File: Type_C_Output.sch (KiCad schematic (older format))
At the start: 38 parts, among them J1 USB_C_Receptacle_USB2.0, Q18 VBA2625, Q19 VBA2625, Q20 VBA2625, Q21 2n7002K, U12 STUSB4700

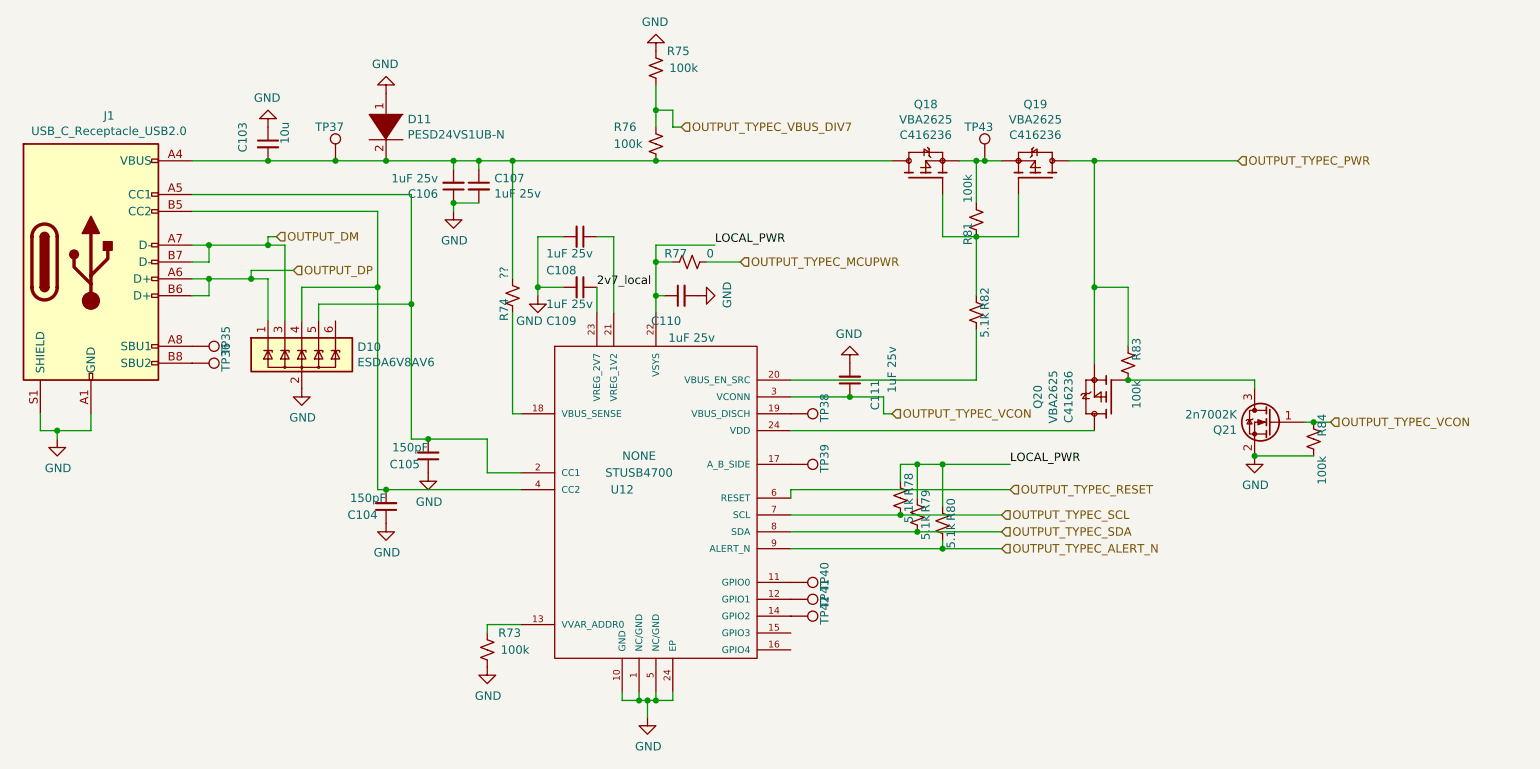
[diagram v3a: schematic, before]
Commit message: Almost connected MCU + ESP32 added leds addedd uart usb cleaned up type-c I/O -- STILL NEED TO level shift I2C
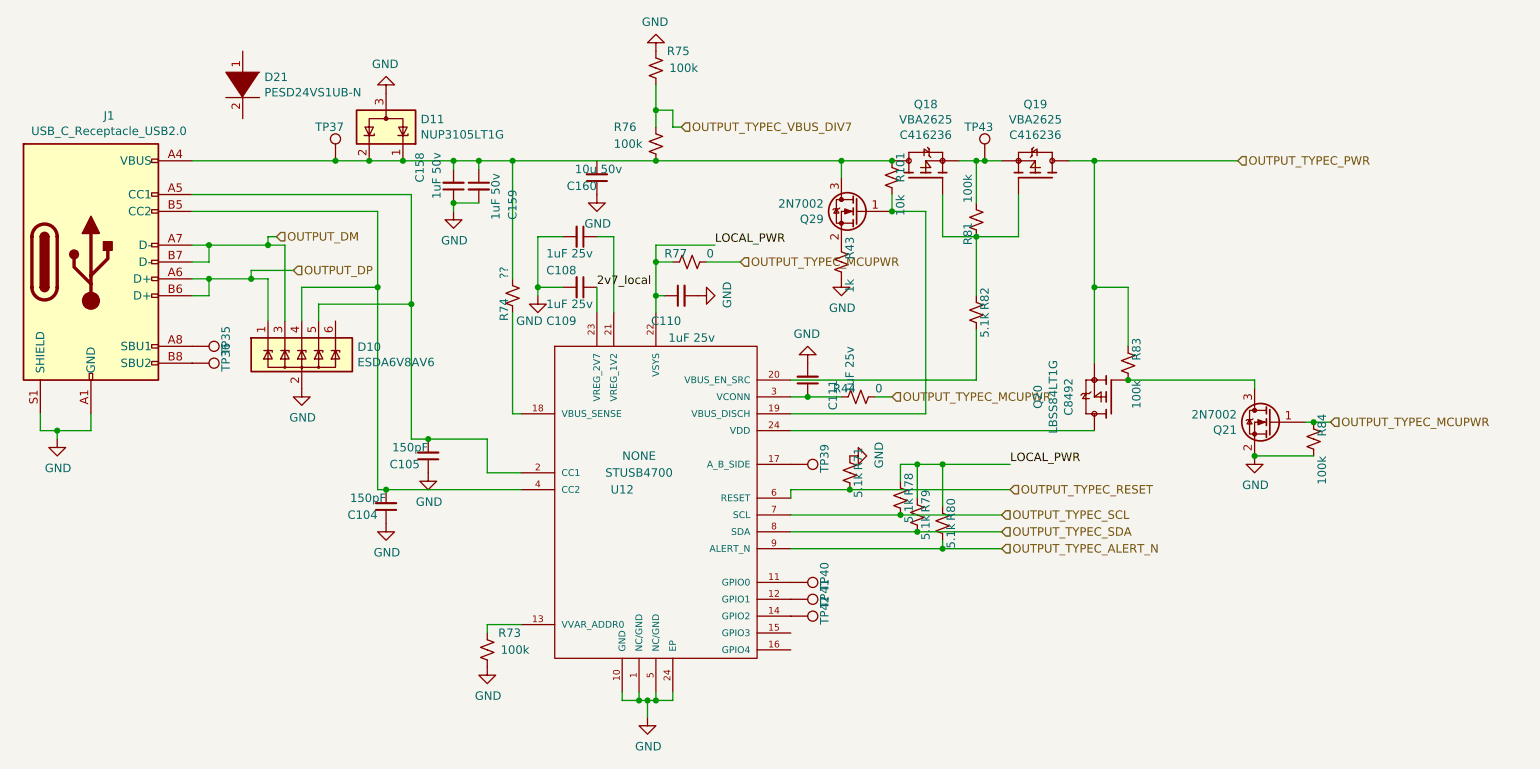
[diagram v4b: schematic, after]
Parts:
- removed C103: 10u, lc_lib:0805_C, symbol Device:C_Small
- removed C106, C107: 1uF 25v, lc_lib:0402_C, symbol Device:C_Small
- removed D11: PESD24VS1UB-N, lc_lib:SOD-523, symbol pspice:DIODE
- removed TP38: TestPoint, TestPoint:TestPoint_Pad_D2.0mm, symbol Connector:TestPoint
- added C158, C159: 1uF 50v, lc_lib:0603_C, symbol Device:C_Small
- added C160: 10u 50v, lc_lib:0805_C, symbol Device:C_Small
- added D11: NUP3105LT1G, Package_TO_SOT_SMD:SOT-23, symbol Power_Protection:SP0502BAJT
- added D21: PESD24VS1UB-N, lc_lib:SOD-523, symbol pspice:DIODE
- added Q29: 2N7002, Package_TO_SOT_SMD:SOT-23, symbol Device:Q_NMOS_GSD
- added R101: 10k, lc_lib:0402_R, symbol Device:R_Small_US
- added R43: 1k, lc_lib:0402_R, symbol Device:R_Small_US
- added R44: 0, lc_lib:0402_R, symbol Device:R_Small_US
- added R71: 5.1k, lc_lib:0402_R, symbol Device:R_Small_US
- Q20: value VBA2625 -> LBSS84LT1G; footprint SmartBattery:SOIC127P600X175-8N -> lc_lib:SOT-23(SOT-23-3); MANUFACTURER Alpha & Omega Semiconductor -> (none); MAXIMUM_PACKAGE_HEIGHT 1.75 mm -> (none); PARTREV I -> (none); STANDARD IPC 7351B -> (none); lcsc C416236 -> C8492
- Q21: value 2n7002K -> 2N7002; LCSC (none) -> C8545
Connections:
- net GND: now also C158.1, C159.2, C160.1, D11.3 (A), R43.1, R71.2
- net OUTPUT_TYPEC_MCUPWR: now also Q21.1 (G), R84.2, R44.1
- net OUTPUT_TYPEC_RESET: now also R71.1
- net at J1.A4 (VBUS), J1.A9 (VBUS), J1.B4 (VBUS)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: now also C158.2, C159.1, D11.1 (K), D11.2 (K), Q29.3 (D), R101.2
- net at U12.19 (VBUS_DISCH): now also Q29.1 (G), R101.1
- net OUTPUT_TYPEC_VCON: no longer names the net of C111.1, U12.3 (VCONN)
- net OUTPUT_TYPEC_VCON: now also R44.2; no longer Q21.1 (G), R84.2
- new net: Q29.2 (S), R43.2
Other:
- moved on the sheet: C111

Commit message: lots of GPIO connectivity changes. fixed no PD on input fixed CH340G leakage. can otherwise power from GPIO. added fet for powering VCONN from 3v/5v NEED TO ADD OVERCURRENT
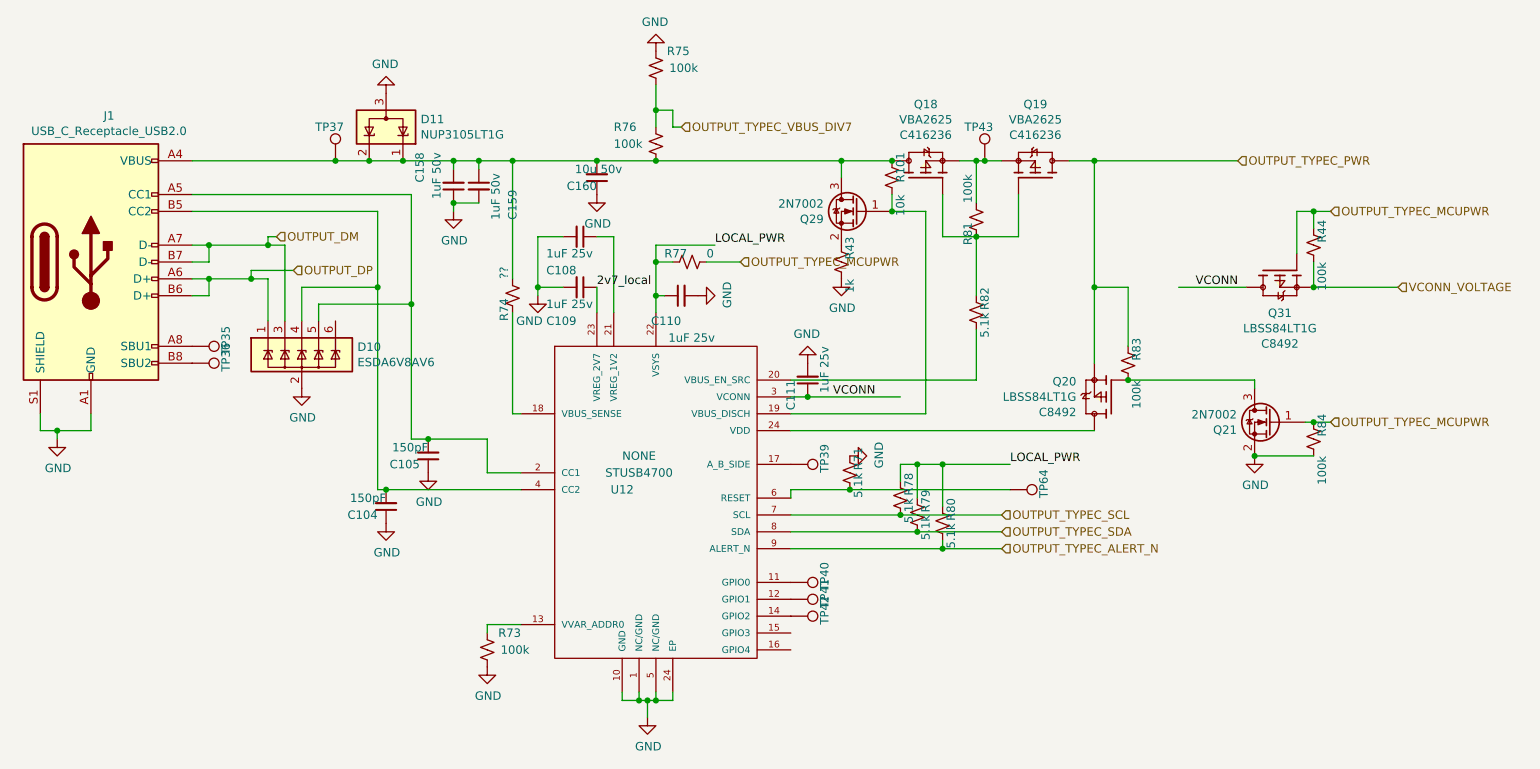
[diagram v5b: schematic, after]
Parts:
- removed D21: PESD24VS1UB-N, lc_lib:SOD-523, symbol pspice:DIODE
- removed Q20: LBSS84LT1G, lc_lib:SOT-23(SOT-23-3), symbol SmartBattery:VBA2625
- added Q20, Q31: LBSS84LT1G, lc_lib:SOT-23(SOT-23-3), symbol SmartBattery:LBSS84LT1G
- added TP64: TestPoint, TestPoint:TestPoint_Pad_D2.0mm, symbol Connector:TestPoint
- R44: value 0 -> 100k; LCSC (none) -> C25741
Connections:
- net OUTPUT_TYPEC_MCUPWR: now also R44.2, Q31.1; no longer R44.1
- net OUTPUT_TYPEC_PWR: now also Q20.2
- net at C158.2, C159.1, D11.1 (K)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: now also C160.2
- net VCONN: now reaches C111.1, U12.3 (VCONN)
- net VCONN: now also Q31.3; no longer R44.2
- net at Q21.3 (D), R83.1: now also Q20.1
- net OUTPUT_TYPEC_RESET: no longer names the net of R71.1, U12.6 (RESET)
- net OUTPUT_TYPEC_RESET: now also TP64.1
- new net: Q20.3, U12.24 (VDD)
- new net VCONN_VOLTAGE: Q31.2, R44.1
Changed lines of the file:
@@
 Connection ~ 4050 1550
 Wire Wire Line
-	4050 1550 4900 1550
+	4050 1550 4550 1550
 Wire Wire Line
 	3850 1600 3850 1550
@@
 Wire Wire Line
 	5700 3150 7500 3150
-$Comp
-L SmartBattery:VBA2625 Q?
-U 1 1 60201E98
-P 7600 2950
-AR Path="/5FF971C1/60201E98" Ref="Q?"  Part="1"
-AR Path="/600C8F88/60201E98" Ref="Q20"  Part="1"
-F 0 "Q20" V 8035 2950 50  0000 C CNN
-F 1 "LBSS84LT1G" V 7944 2950 50  0000 C CNN
-F 2 "lc_lib:SOT-23(SOT-23-3)" H 7600 2950 50  0001 L BNN
-F 3 "" H 7600 2950 50  0001 L BNN
-F 4 "" H 7600 2950 50  0001 L BNN "MANUFACTURER"
-F 5 "" H 7600 2950 50  0001 L BNN "PARTREV"
-F 6 "" H 7600 2950 50  0001 L BNN "STANDARD"
-F 7 "" H 7600 2950 50  0001 L BNN "MAXIMUM_PACKAGE_HEIGHT"
-F 8 "C8492" V 7853 2950 50  0000 C CNN "lcsc"
-	1    7600 2950
-	-1   0    0    -1
-$EndComp
 Text Label 5250 2050 0    50   ~ 0
 LOCAL_PWR
@@
 Wire Wire Line
 	5700 3650 6350 3650
-Text HLabel 7000 3500 2    50   Input ~ 0
-OUTPUT_TYPEC_RESET
 Wire Wire Line
 	7000 3500 6050 3500
@@
 AR Path="/5FF971C1/60269C14" Ref="C?"  Part="1"
 AR Path="/600C8F88/60269C14" Ref="C111"  Part="1"
-F 0 "C111" V 5650 2850 50  0000 L CNN
-F 1 "1uF 25v" V 5550 2650 50  0000 L CNN
+F 0 "C111" V 5900 2850 50  0000 L CNN
+F 1 "1uF 25v" V 5700 2650 50  0000 L CNN
 F 2 "lc_lib:0402_C" H 5800 2850 50  0001 C CNN
 F 3 "~" H 5800 2850 50  0001 C CNN
@@
 $EndComp
 Connection ~ 5800 2950
-Wire Wire Line
-	5800 2950 6000 2950
 $Comp
 L power:GND #PWR?
@@
 	-1   0    0    1
 $EndComp
-Text HLabel 6300 2950 2    50   Input ~ 0
+Text HLabel 8900 1850 2    50   Input ~ 0
 OUTPUT_TYPEC_MCUPWR
 Wire Wire Line
@@
 Wire Wire Line
 	8450 2850 8450 2900
-Connection ~ 7700 2850
 $Comp
 L power:GND #PWR?
@@
 Connection ~ 3400 1550
 $Comp
-L Device:R_Small_US R?
-U 1 1 60344C8C
-P 6100 2950
-AR Path="/5FD99B08/60344C8C" Ref="R?"  Part="1"
-AR Path="/5FF1D194/60344C8C" Ref="R?"  Part="1"
-AR Path="/600C8F88/60344C8C" Ref="R44"  Part="1"
-F 0 "R44" V 6050 2800 50  0000 L CNN
-F 1 "0" V 6050 3050 50  0000 L CNN
-F 2 "lc_lib:0402_R" H 6100 2950 50  0001 C CNN
-F 3 "~" H 6100 2950 50  0001 C CNN
-	1    6100 2950
-	0    1    1    0
-$EndComp
-$Comp
 L Device:Q_NMOS_GSD Q?
 U 1 1 6034DD17
@@
 $EndComp
 Wire Wire Line
-	6200 2950 6300 2950
-Wire Wire Line
 	5700 3050 6500 3050
 Wire Wire Line
@@
 	1    3900 3250
 	1    0    0    -1
-$EndComp
-$Comp
-L pspice:DIODE D?
-U 1 1 60206BB7
-P 2450 1100
-AR Path="/5FF971C1/60206BB7" Ref="D?"  Part="1"
-AR Path="/600C8F88/60206BB7" Ref="D21"  Part="1"
-F 0 "D21" V 2404 1228 50  0000 L CNN
-F 1 "PESD24VS1UB-N" V 2495 1228 50  0000 L CNN
-F 2 "lc_lib:SOD-523" H 2450 1100 50  0001 C CNN
-F 3 "~" H 2450 1100 50  0001 C CNN
-F 4 "C316036" V 2450 1100 50  0001 C CNN "lcsc"
-	1    2450 1100
-	0    1    1    0
 $EndComp
 $Comp
@@
 	0    -1   -1   0
 $EndComp
+$Comp
+L Connector:TestPoint TP?
+U 1 1 6026B3C6
+P 7000 3500
+AR Path="/5FD15753/6026B3C6" Ref="TP?"  Part="1"
+AR Path="/5FD99B08/6026B3C6" Ref="TP?"  Part="1"
+AR Path="/5FF971C1/6026B3C6" Ref="TP?"  Part="1"
+AR Path="/600C8F88/6026B3C6" Ref="TP64"  Part="1"
+F 0 "TP64" H 7050 3700 50  0000 R CNN
+F 1 "TestPoint" H 6450 3550 50  0001 R CNN
+F 2 "TestPoint:TestPoint_Pad_D2.0mm" H 7200 3500 50  0001 C CNN
+F 3 "~" H 7200 3500 50  0001 C CNN
+	1    7000 3500
+	0    1    1    0
+$EndComp
+Connection ~ 4550 1550
+Wire Wire Line
+	4550 1550 4900 1550
+Wire Wire Line
+	5800 2950 6350 2950
+Text HLabel 9300 2300 2    50   Input ~ 0
+VCONN_VOLTAGE
+Text Label 5950 2950 0    50   ~ 0
+VCONN
+Wire Wire Line
+	8400 2300 8000 2300
+Text Label 8100 2300 0    50   ~ 0
+VCONN
+$Comp
+L SmartBattery:LBSS84LT1G Q20
+U 1 1 6036965C
+P 7600 2950
+F 0 "Q20" H 7807 3041 50  0000 L CNN
+F 1 "LBSS84LT1G" H 7807 2950 50  0000 L CNN
+F 2 "lc_lib:SOT-23(SOT-23-3)" H 7600 2950 50  0001 L BNN
+F 3 "" H 7600 2950 50  0001 L BNN
+F 4 "I" H 7600 2950 50  0001 L BNN "PARTREV"
+F 5 "IPC 7351B" H 7600 2950 50  0001 L BNN "STANDARD"
+F 6 "1.11 mm" H 7600 2950 50  0001 L BNN "MAXIMUM_PACKAGE_HEIGHT"
+F 7 "C8492" H 7807 2859 50  0000 L CNN "lcsc"
+	1    7600 2950
+	-1   0    0    -1
+$EndComp
+$Comp
+L SmartBattery:LBSS84LT1G Q31
+U 1 1 6036CF55
+P 8600 2200
+F 0 "Q31" V 8853 2200 50  0000 C CNN
+F 1 "LBSS84LT1G" V 8944 2200 50  0000 C CNN
+F 2 "lc_lib:SOT-23(SOT-23-3)" H 8600 2200 50  0001 L BNN
+F 3 "" H 8600 2200 50  0001 L BNN
+F 4 "I" H 8600 2200 50  0001 L BNN "PARTREV"
+F 5 "IPC 7351B" H 8600 2200 50  0001 L BNN "STANDARD"
+F 6 "1.11 mm" H 8600 2200 50  0001 L BNN "MAXIMUM_PACKAGE_HEIGHT"
+F 7 "C8492" V 9035 2200 50  0000 C CNN "lcsc"
+	1    8600 2200
+	0    1    1    0
+$EndComp
+Connection ~ 7700 2850
+Wire Wire Line
+	8700 2100 8700 1850
+Wire Wire Line
+	8700 1850 8800 1850
+Wire Wire Line
+	9300 2300 8800 2300
+$Comp
+L Device:R_Small_US R?
+U 1 1 60392469
+P 8800 2050
+AR Path="/5FD99B08/60392469" Ref="R?"  Part="1"
+AR Path="/5FF1D194/60392469" Ref="R?"  Part="1"
+AR Path="/5FF971C1/60392469" Ref="R?"  Part="1"
+AR Path="/600C8F88/60392469" Ref="R44"  Part="1"
+F 0 "R44" V 8750 1900 50  0000 L CNN
+F 1 "100k" V 8750 2150 50  0000 L CNN
+F 2 "lc_lib:0402_R" H 8800 2050 50  0001 C CNN
+F 3 "~" H 8800 2050 50  0001 C CNN
+F 4 "C25741" V 8800 2050 50  0001 C CNN "LCSC"
+	1    8800 2050
+	-1   0    0    1
+$EndComp
+Wire Wire Line
+	8800 1950 8800 1850
+Connection ~ 8800 1850
+Wire Wire Line
+	8800 1850 8900 1850
+Wire Wire Line
+	8800 2300 8800 2150
+Connection ~ 8800 2300
 $EndSCHEMATC

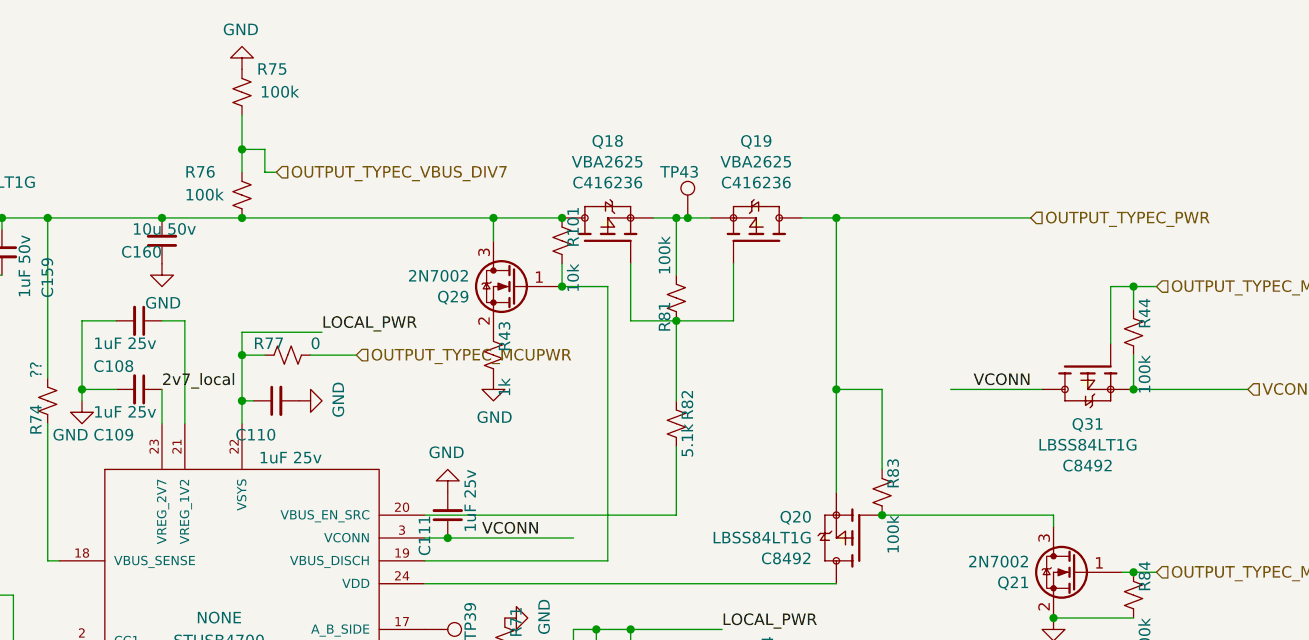
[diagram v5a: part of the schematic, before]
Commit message: Modified connections, added current limit
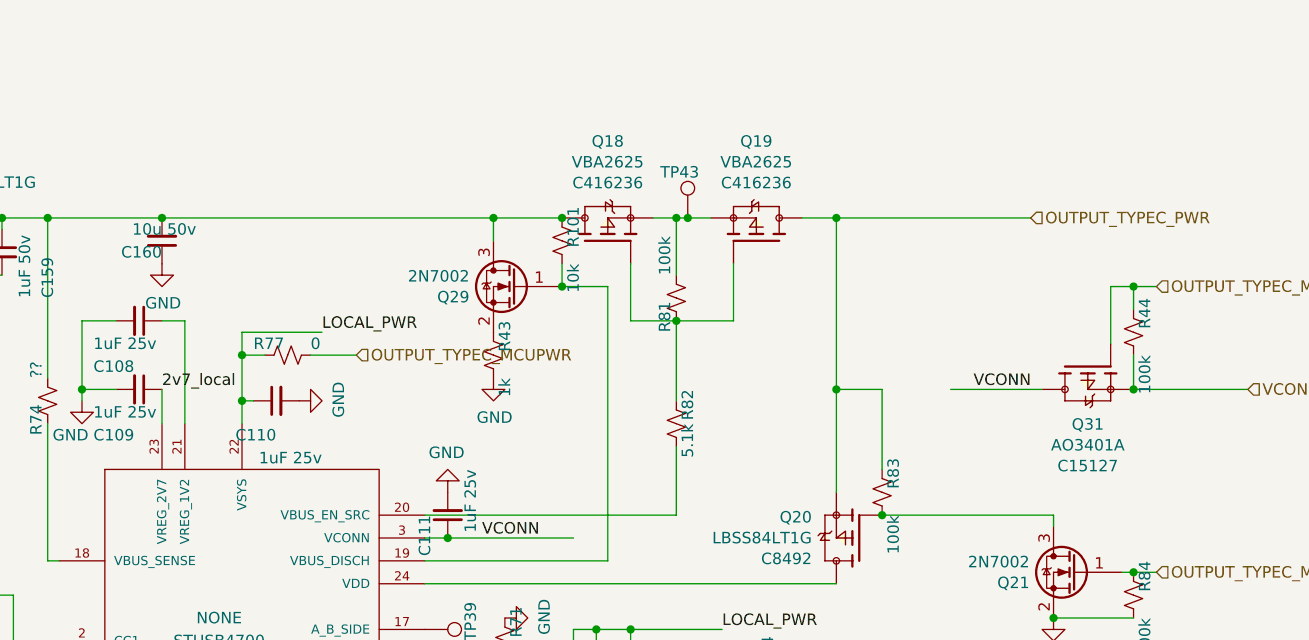
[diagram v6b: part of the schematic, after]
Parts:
- removed R75, R76: 100k, lc_lib:0402_R, symbol Device:R_Small_US
- Q31: value LBSS84LT1G -> AO3401A; MAXIMUM_PACKAGE_HEIGHT 1.11 mm -> (none); lcsc C8492 -> C15127
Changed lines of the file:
@@
-$Comp
-L Device:R_Small_US R?
-U 1 1 6010780A
-P 4900 1450
-AR Path="/5FD99B08/6010780A" Ref="R?"  Part="1"
-AR Path="/5FF1D194/6010780A" Ref="R?"  Part="1"
-AR Path="/5FF971C1/6010780A" Ref="R?"  Part="1"
-AR Path="/600C8F88/6010780A" Ref="R76"  Part="1"
-F 0 "R76" H 4650 1550 50  0000 L CNN
-F 1 "100k" H 4650 1450 50  0000 L CNN
-F 2 "lc_lib:0402_R" H 4900 1450 50  0001 C CNN
-F 3 "~" H 4900 1450 50  0001 C CNN
-F 4 "C25741" V 4900 1450 50  0001 C CNN "LCSC"
-	1    4900 1450
-	1    0    0    -1
-$EndComp
-Connection ~ 4900 1550
-$Comp
-L Device:R_Small_US R?
-U 1 1 60107813
-P 4900 1000
-AR Path="/5FD99B08/60107813" Ref="R?"  Part="1"
-AR Path="/5FF1D194/60107813" Ref="R?"  Part="1"
-AR Path="/5FF971C1/60107813" Ref="R?"  Part="1"
-AR Path="/600C8F88/60107813" Ref="R75"  Part="1"
-F 0 "R75" H 4700 900 50  0000 L CNN
-F 1 "100k" H 4650 1000 50  0000 L CNN
-F 2 "lc_lib:0402_R" H 4900 1000 50  0001 C CNN
-F 3 "~" H 4900 1000 50  0001 C CNN
-F 4 "C25741" V 4900 1000 50  0001 C CNN "LCSC"
-	1    4900 1000
-	-1   0    0    1
-$EndComp
-Wire Wire Line
-	4900 1350 4900 1250
-$Comp
-L power:GND #PWR?
-U 1 1 6010781A
-P 4900 900
-AR Path="/5FF971C1/6010781A" Ref="#PWR?"  Part="1"
-AR Path="/600C8F88/6010781A" Ref="#PWR0193"  Part="1"
-F 0 "#PWR0193" H 4900 650 50  0001 C CNN
-F 1 "GND" H 4905 727 50  0000 C CNN
-F 2 "" H 4900 900 50  0001 C CNN
-F 3 "" H 4900 900 50  0001 C CNN
-	1    4900 900
-	-1   0    0    1
-$EndComp
-Wire Wire Line
-	4900 1250 5000 1250
-Wire Wire Line
-	5000 1250 5000 1350
-Connection ~ 4900 1250
-Wire Wire Line
-	4900 1250 4900 1100
-Wire Wire Line
-	5000 1350 5050 1350
-Text HLabel 5050 1350 2    50   Input ~ 0
-OUTPUT_TYPEC_VBUS_DIV7
 $Comp
 L Device:R_Small_US R?
@@
 Wire Wire Line
 	3300 3500 3250 3500
-Wire Wire Line
-	4900 1550 6000 1550
 Wire Wire Line
 	4100 3050 4050 3050
@@
 Connection ~ 4550 1550
 Wire Wire Line
-	4550 1550 4900 1550
-Wire Wire Line
 	5800 2950 6350 2950
 Text HLabel 9300 2300 2    50   Input ~ 0
@@
 P 8600 2200
 F 0 "Q31" V 8853 2200 50  0000 C CNN
-F 1 "LBSS84LT1G" V 8944 2200 50  0000 C CNN
+F 1 "AO3401A" V 8944 2200 50  0000 C CNN
 F 2 "lc_lib:SOT-23(SOT-23-3)" H 8600 2200 50  0001 L BNN
 F 3 "" H 8600 2200 50  0001 L BNN
 F 4 "I" H 8600 2200 50  0001 L BNN "PARTREV"
 F 5 "IPC 7351B" H 8600 2200 50  0001 L BNN "STANDARD"
-F 6 "1.11 mm" H 8600 2200 50  0001 L BNN "MAXIMUM_PACKAGE_HEIGHT"
-F 7 "C8492" V 9035 2200 50  0000 C CNN "lcsc"
+F 6 "" H 8600 2200 50  0001 L BNN "MAXIMUM_PACKAGE_HEIGHT"
+F 7 "C15127" V 9035 2200 50  0000 C CNN "lcsc"
 	1    8600 2200
 	0    1    1    0
@@
 	8800 2300 8800 2150
 Connection ~ 8800 2300
+Wire Wire Line
+	4550 1550 6000 1550
 $EndSCHEMATC
